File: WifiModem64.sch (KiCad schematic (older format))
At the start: 4 parts, among them J1 C64-UserPort, J2 PWR1, U1 WeMos_mini, U2 WeMos_D1_mini_OLED_Shield

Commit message: WiP.
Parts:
- removed J2: PWR1, Pin_Headers:Pin_Header_Straight_1x02_Pitch2.54mm, symbol Conn_01x02
- added JP1: IntPwr, Connectors:GS2, symbol Jumper_NC_Small
- added JP2: CTS, Connectors:GS2, symbol Jumper_NC_Small
- added JP3: RTS, Connectors:GS2, symbol Jumper_NC_Small
- added JP4: SP1, Connectors:GS2, symbol Jumper_NC_Small
- added JP5: SP2, Connectors:GS2, symbol Jumper_NC_Small
- added Q1, Q2, Q3, Q4: BSS138, TO_SOT_Packages_SMD:SOT-23, symbol BSS138
- added R1, R2, R3, R4, R5, R6, R7, R8: 10k, Resistors_SMD:R_0805_HandSoldering, symbol R
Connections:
- net labels added: +3V3, CTS, RTS, SP1, SP2
- net labels removed: W_3V3, W_5V, W_GND
- wire segments 27 -> 71
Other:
- moved on the sheet: J1

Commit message: WiP.
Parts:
- added SW1: Push, Buttons_Switches_THT:SW_Tactile_SPST_Angled_PTS645Vx58-2LFS, symbol SW_Push
- added SW2: Reset, Buttons_Switches_THT:SW_Tactile_SPST_Angled_PTS645Vx58-2LFS, symbol SW_Push
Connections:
- net GND: now also SW1.2, SW2.2
- net W_D3: now also SW1.1
- net RST: now reaches J1.3 (/RST)
- net RST: now also SW2.1
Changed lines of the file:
@@
 	1    0    0    -1
 $EndComp
-Wire Wire Line
-	6550 3550 7200 3550
 $Comp
 L +5V #PWR03
@@
 	1    0    0    -1
 $EndComp
-Wire Wire Line
-	5500 3650 5550 3650
-Wire Wire Line
-	5450 3550 5550 3550
-Wire Wire Line
-	5550 4350 5150 4350
-Wire Wire Line
-	5150 4350 5150 4900
-Wire Wire Line
-	5150 4900 6650 4900
-Wire Wire Line
-	6650 4900 6650 3950
-Wire Wire Line
-	6650 3950 6550 3950
-Wire Wire Line
-	6550 3850 6700 3850
-Wire Wire Line
-	6700 4050 6550 4050
-Wire Wire Line
-	5400 4600 5400 4550
-Wire Wire Line
-	5400 4550 5550 4550
 $Comp
 L WeMos_D1_mini_OLED_Shield U2
@@
 Text GLabel 5450 3550 0    39   Input ~ 0
 SP2
-Wire Wire Line
-	5500 3650 5500 3550
-Connection ~ 5500 3550
 Text GLabel 5450 4250 0    39   Input ~ 0
 RTS
-Wire Wire Line
-	5450 4250 5550 4250
 Text GLabel 5450 3750 0    39   Input ~ 0
 CTS
-Wire Wire Line
-	5450 3750 5550 3750
 Text GLabel 6700 4050 2    39   Input ~ 0
 SP2
 Text GLabel 5450 4450 0    39   Input ~ 0
 SP1
-Wire Wire Line
-	5450 4450 5550 4450
 Text GLabel 6700 3850 2    39   Input ~ 0
 SP1
-Wire Wire Line
-	6550 4550 6550 4650
-Wire Wire Line
-	6550 4650 5500 4650
-Wire Wire Line
-	5500 4650 5500 4550
-Connection ~ 5500 4550
-Wire Wire Line
-	6550 3300 6550 3450
-Wire Wire Line
-	5450 3300 6550 3300
-Wire Wire Line
-	5550 3300 5550 3450
 $Comp
 L GND #PWR05
@@
 	1    0    0    -1
 $EndComp
-Connection ~ 5550 3300
 $Comp
 L Jumper_NC_Small JP1
@@
 	1    0    0    -1
 $EndComp
-Wire Wire Line
-	7400 3550 7400 3450
 $Comp
 L +3V3 #PWR06
@@
 	1    0    0    -1
 $EndComp
-Wire Wire Line
-	3700 1450 3800 1450
-Wire Wire Line
-	3800 1450 3800 1400
 $Comp
 L +3V3 #PWR07
@@
 	1    0    0    -1
 $EndComp
-Wire Wire Line
-	5750 1450 5850 1450
-Wire Wire Line
-	5850 1450 5850 1400
-Wire Wire Line
-	2700 1550 2350 1550
-Wire Wire Line
-	2350 1550 2350 1600
-Wire Wire Line
-	2700 1450 2600 1450
-Wire Wire Line
-	2600 1450 2600 1400
 $Comp
 L +5V #PWR08
@@
 	1    0    0    -1
 $EndComp
-Wire Wire Line
-	4750 1450 4650 1450
-Wire Wire Line
-	4650 1450 4650 1400
 $Comp
 L GND #PWR09
@@
 	1    0    0    -1
 $EndComp
-Wire Wire Line
-	4750 1550 4400 1550
-Wire Wire Line
-	4400 1550 4400 1600
 $Comp
 L Jumper_NC_Small JP5
@@
 Text GLabel 9700 6000 0    39   Input ~ 0
 SP2
-Wire Wire Line
-	9700 6000 9800 6000
 Text GLabel 10350 6000 2    39   Input ~ 0
 W_TX
-Wire Wire Line
-	10000 6000 10350 6000
 $Comp
 L BSS138 Q4
@@
 	1    0    0    -1
 $EndComp
-Wire Wire Line
-	9750 5650 9800 5650
-Wire Wire Line
-	10200 5650 10250 5650
-Wire Wire Line
-	9750 5350 10000 5350
 $Comp
 L +3V3 #PWR010
@@
 	1    0    0    -1
 $EndComp
-Wire Wire Line
-	9750 5350 9750 5300
-Wire Wire Line
-	10250 5300 10250 5350
-Wire Wire Line
-	9750 5650 9750 6000
-Connection ~ 9750 6000
-Wire Wire Line
-	10250 5650 10250 6000
-Connection ~ 10250 6000
 $Comp
 L Jumper_NC_Small JP4
@@
 Text GLabel 9700 4950 0    39   Input ~ 0
 SP1
-Wire Wire Line
-	9700 4950 9800 4950
 Text GLabel 10350 4950 2    39   Input ~ 0
 W_RX
-Wire Wire Line
-	10000 4950 10350 4950
 $Comp
 L BSS138 Q3
@@
 	1    0    0    -1
 $EndComp
-Wire Wire Line
-	9750 4600 9800 4600
-Wire Wire Line
-	10200 4600 10250 4600
-Wire Wire Line
-	9750 4300 10000 4300
 $Comp
 L +3V3 #PWR012
@@
 	1    0    0    -1
 $EndComp
-Wire Wire Line
-	9750 4300 9750 4250
-Wire Wire Line
-	10250 4250 10250 4300
-Wire Wire Line
-	9750 4600 9750 4950
-Connection ~ 9750 4950
-Wire Wire Line
-	10250 4600 10250 4950
-Connection ~ 10250 4950
 $Comp
 L Jumper_NC_Small JP3
@@
 Text GLabel 9700 3900 0    39   Input ~ 0
 RTS
-Wire Wire Line
-	9700 3900 9800 3900
 Text GLabel 10350 3900 2    39   Input ~ 0
 W_D7
-Wire Wire Line
-	10000 3900 10350 3900
 $Comp
 L BSS138 Q2
@@
 	1    0    0    -1
 $EndComp
-Wire Wire Line
-	9750 3550 9800 3550
-Wire Wire Line
-	10200 3550 10250 3550
-Wire Wire Line
-	9750 3250 10000 3250
 $Comp
 L +3V3 #PWR014
@@
 	1    0    0    -1
 $EndComp
-Wire Wire Line
-	9750 3250 9750 3200
-Wire Wire Line
-	10250 3200 10250 3250
-Wire Wire Line
-	9750 3550 9750 3900
-Connection ~ 9750 3900
-Wire Wire Line
-	10250 3550 10250 3900
-Connection ~ 10250 3900
 $Comp
 L Jumper_NC_Small JP2
@@
 Text GLabel 9700 2850 0    39   Input ~ 0
 CTS
-Wire Wire Line
-	9700 2850 9800 2850
 Text GLabel 10350 2850 2    39   Input ~ 0
 W_D6
-Wire Wire Line
-	10000 2850 10350 2850
 $Comp
 L BSS138 Q1
@@
 	1    0    0    -1
 $EndComp
-Wire Wire Line
-	9750 2500 9800 2500
-Wire Wire Line
-	10200 2500 10250 2500
-Wire Wire Line
-	9750 2200 10000 2200
 $Comp
 L +3V3 #PWR016
@@
 	1    0    0    -1
 $EndComp
+$Comp
+L SW_Push SW1
+U 1 1 5A3679A2
+P 10050 1200
+F 0 "SW1" H 10100 1300 50  0000 L CNN
+F 1 "Push" H 10050 1140 50  0000 C CNN
+F 2 "Buttons_Switches_THT:SW_Tactile_SPST_Angled_PTS645Vx58-2LFS" H 10050 1400 50  0001 C CNN
+F 3 "" H 10050 1400 50  0001 C CNN
+	1    10050 1200
+	1    0    0    -1
+$EndComp
+Text GLabel 9750 1200 0    39   Input ~ 0
+W_D3
+$Comp
+L GND #PWR018
+U 1 1 5A367D37
+P 10350 1550
+F 0 "#PWR018" H 10350 1300 50  0001 C CNN
+F 1 "GND" H 10350 1400 50  0000 C CNN
+F 2 "" H 10350 1550 50  0001 C CNN
+F 3 "" H 10350 1550 50  0001 C CNN
+	1    10350 1550
+	1    0    0    -1
+$EndComp
+$Comp
+L SW_Push SW2
+U 1 1 5A36803A
+P 10050 1500
+F 0 "SW2" H 10100 1600 50  0000 L CNN
+F 1 "Reset" H 10050 1440 50  0000 C CNN
+F 2 "Buttons_Switches_THT:SW_Tactile_SPST_Angled_PTS645Vx58-2LFS" H 10050 1700 50  0001 C CNN
+F 3 "" H 10050 1700 50  0001 C CNN
+	1    10050 1500
+	1    0    0    -1
+$EndComp
+Wire Wire Line
+	6550 3550 7200 3550
+Wire Wire Line
+	5500 3650 5550 3650
+Wire Wire Line
+	5450 3550 5550 3550
+Wire Wire Line
+	5550 4350 5150 4350
+Wire Wire Line
+	5150 4350 5150 4900
+Wire Wire Line
+	5150 4900 6650 4900
+Wire Wire Line
+	6650 4900 6650 3950
+Wire Wire Line
+	6650 3950 6550 3950
+Wire Wire Line
+	6550 3850 6700 3850
+Wire Wire Line
+	6700 4050 6550 4050
+Wire Wire Line
+	5400 4600 5400 4550
+Wire Wire Line
+	5400 4550 5550 4550
+Wire Wire Line
+	5500 3650 5500 3550
+Connection ~ 5500 3550
+Wire Wire Line
+	5450 4250 5550 4250
+Wire Wire Line
+	5450 3750 5550 3750
+Wire Wire Line
+	5450 4450 5550 4450
+Wire Wire Line
+	6550 4550 6550 4650
+Wire Wire Line
+	6550 4650 5500 4650
+Wire Wire Line
+	5500 4650 5500 4550
+Connection ~ 5500 4550
+Wire Wire Line
+	6550 3300 6550 3450
+Wire Wire Line
+	5450 3300 6550 3300
+Wire Wire Line
+	5550 3300 5550 3450
+Connection ~ 5550 3300
+Wire Wire Line
+	7400 3550 7400 3450
+Wire Wire Line
+	3700 1450 3800 1450
+Wire Wire Line
+	3800 1450 3800 1400
+Wire Wire Line
+	5750 1450 5850 1450
+Wire Wire Line
+	5850 1450 5850 1400
+Wire Wire Line
+	2700 1550 2350 1550
+Wire Wire Line
+	2350 1550 2350 1600
+Wire Wire Line
+	2700 1450 2600 1450
+Wire Wire Line
+	2600 1450 2600 1400
+Wire Wire Line
+	4750 1450 4650 1450
+Wire Wire Line
+	4650 1450 4650 1400
+Wire Wire Line
+	4750 1550 4400 1550
+Wire Wire Line
+	4400 1550 4400 1600
+Wire Wire Line
+	9700 6000 9800 6000
+Wire Wire Line
+	10000 6000 10350 6000
+Wire Wire Line
+	9750 5650 9800 5650
+Wire Wire Line
+	10200 5650 10250 5650
+Wire Wire Line
+	9750 5350 10000 5350
+Wire Wire Line
+	9750 5350 9750 5300
+Wire Wire Line
+	10250 5300 10250 5350
+Wire Wire Line
+	9750 5650 9750 6000
+Connection ~ 9750 6000
+Wire Wire Line
+	10250 5650 10250 6000
+Connection ~ 10250 6000
+Wire Wire Line
+	9700 4950 9800 4950
+Wire Wire Line
+	10000 4950 10350 4950
+Wire Wire Line
+	9750 4600 9800 4600
+Wire Wire Line
+	10200 4600 10250 4600
+Wire Wire Line
+	9750 4300 10000 4300
+Wire Wire Line
+	9750 4300 9750 4250
+Wire Wire Line
+	10250 4250 10250 4300
+Wire Wire Line
+	9750 4600 9750 4950
+Connection ~ 9750 4950
+Wire Wire Line
+	10250 4600 10250 4950
+Connection ~ 10250 4950
+Wire Wire Line
+	9700 3900 9800 3900
+Wire Wire Line
+	10000 3900 10350 3900
+Wire Wire Line
+	9750 3550 9800 3550
+Wire Wire Line
+	10200 3550 10250 3550
+Wire Wire Line
+	9750 3250 10000 3250
+Wire Wire Line
+	9750 3250 9750 3200
+Wire Wire Line
+	10250 3200 10250 3250
+Wire Wire Line
+	9750 3550 9750 3900
+Connection ~ 9750 3900
+Wire Wire Line
+	10250 3550 10250 3900
+Connection ~ 10250 3900
+Wire Wire Line
+	9700 2850 9800 2850
+Wire Wire Line
+	10000 2850 10350 2850
+Wire Wire Line
+	9750 2500 9800 2500
+Wire Wire Line
+	10200 2500 10250 2500
+Wire Wire Line
+	9750 2200 10000 2200
 Wire Wire Line
 	9750 2200 9750 2150
@@
 	10250 2500 10250 2850
 Connection ~ 10250 2850
+Wire Wire Line
+	9750 1200 9850 1200
+Wire Wire Line
+	10250 1200 10350 1200
+Wire Wire Line
+	10350 1200 10350 1550
+Wire Wire Line
+	10250 1500 10350 1500
+Connection ~ 10350 1500
+Text GLabel 9750 1500 0    39   Input ~ 0
+RST
+Wire Wire Line
+	9750 1500 9850 1500
+Text GLabel 6700 3650 2    39   Input ~ 0
+RST
+Wire Wire Line
+	6550 3650 6700 3650
 $EndSCHEMATC

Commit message: Added LED and mounting holes.
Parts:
- added C1: 100n, Capacitors_SMD:C_0805_HandSoldering, symbol C
- added LED1: WS2812B, WifiModem64:WS2812B, symbol WS2812B
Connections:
- net +5V: now also C1.1, LED1.1 (VCC)
- net GND: now also C1.2, LED1.3 (GND)
- net W_D0: now also LED1.4 (DIN)
- net W_D7: no longer JP3.2, Q2.3 (D), R6.2
- net W_D8: now also JP3.2, Q2.3 (D), R6.2
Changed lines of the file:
@@
 RTS
 Text GLabel 10350 3900 2    39   Input ~ 0
-W_D7
+W_D8
 $Comp
 L BSS138 Q2
@@
 Wire Wire Line
 	6550 3650 6700 3650
+$Comp
+L GND #PWR019
+U 1 1 5A378519
+P 3800 4150
+F 0 "#PWR019" H 3800 3900 50  0001 C CNN
+F 1 "GND" H 3800 4000 50  0000 C CNN
+F 2 "" H 3800 4150 50  0001 C CNN
+F 3 "" H 3800 4150 50  0001 C CNN
+	1    3800 4150
+	1    0    0    -1
+$EndComp
+$Comp
+L +5V #PWR020
+U 1 1 5A37855B
+P 2500 3750
+F 0 "#PWR020" H 2500 3600 50  0001 C CNN
+F 1 "+5V" H 2500 3890 50  0000 C CNN
+F 2 "" H 2500 3750 50  0001 C CNN
+F 3 "" H 2500 3750 50  0001 C CNN
+	1    2500 3750
+	1    0    0    -1
+$EndComp
+Text GLabel 3650 3750 2    39   Input ~ 0
+W_D0
+$Comp
+L WS2812B LED1
+U 1 1 5A3787C4
+P 3150 3950
+F 0 "LED1" H 3150 3550 60  0000 C CNN
+F 1 "WS2812B" H 3150 4350 60  0000 C CNN
+F 2 "WifiModem64:WS2812B" V 3100 3950 60  0001 C CNN
+F 3 "" V 3100 3950 60  0000 C CNN
+	1    3150 3950
+	1    0    0    -1
+$EndComp
+Wire Wire Line
+	2500 3750 2650 3750
+Wire Wire Line
+	3650 4150 3800 4150
+$Comp
+L C C1
+U 1 1 5A3799FA
+P 2550 3950
+F 0 "C1" H 2575 4050 50  0000 L CNN
+F 1 "100n" H 2575 3850 50  0000 L CNN
+F 2 "Capacitors_SMD:C_0805_HandSoldering" H 2588 3800 50  0001 C CNN
+F 3 "" H 2550 3950 50  0001 C CNN
+	1    2550 3950
+	1    0    0    -1
+$EndComp
+Wire Wire Line
+	2550 3800 2550 3750
+Connection ~ 2550 3750
+Wire Wire Line
+	2550 4100 2550 4450
+Wire Wire Line
+	2550 4450 3700 4450
+Wire Wire Line
+	3700 4450 3700 4150
+Connection ~ 3700 4150
 $EndSCHEMATC

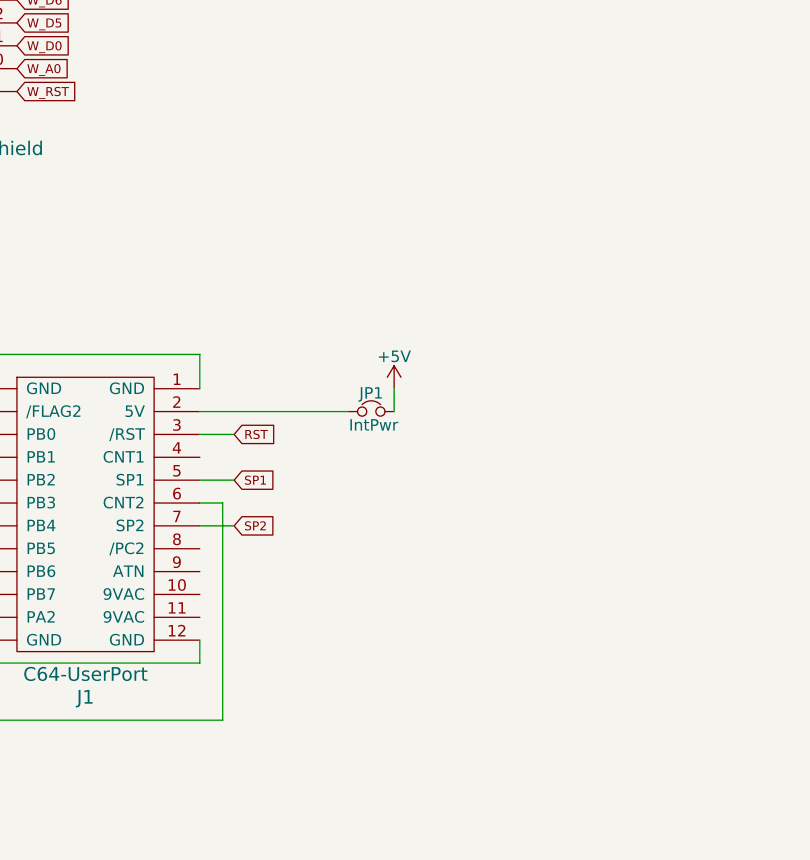
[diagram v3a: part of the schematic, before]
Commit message: Added optional USB power supply.
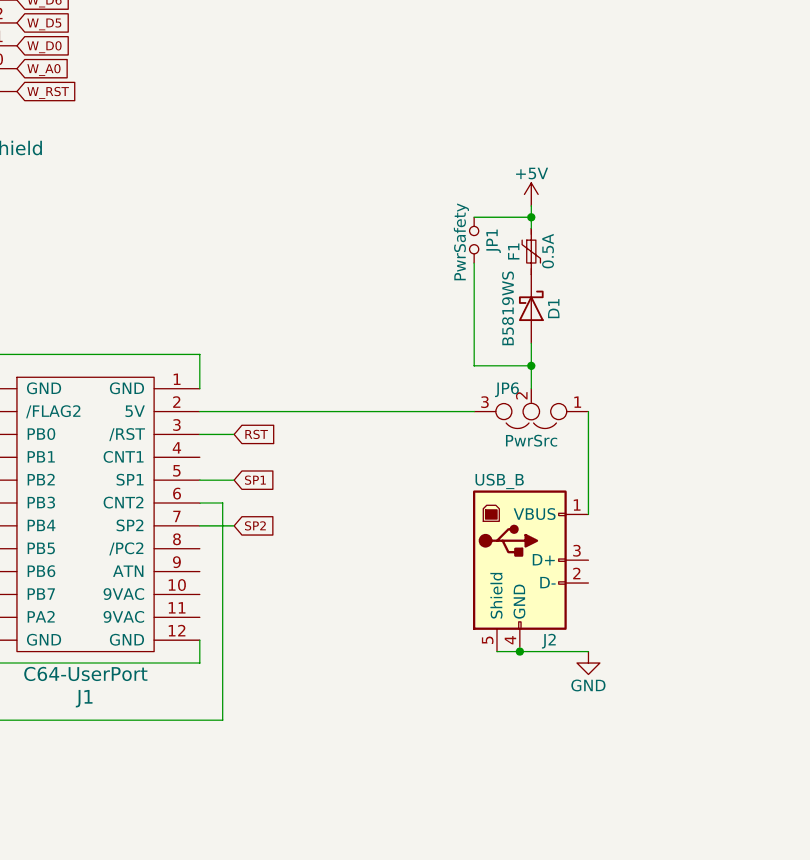
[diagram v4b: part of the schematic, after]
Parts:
- removed JP1: IntPwr, Connectors:GS2, symbol Jumper_NC_Small
- added D1: B5819WS, Diodes_SMD:D_0805, symbol D_Schottky
- added F1: 0.5A, Resistors_SMD:R_1206_HandSoldering, symbol Polyfuse_Small
- added J2: USB_B, Connectors:USB_Micro-B, symbol USB_B
- added JP1: PwrSafety, Connectors:GS2, symbol Jumper_NO_Small
- added JP6: PwrSrc, Pin_Headers:Pin_Header_Straight_1x03_Pitch2.54mm, symbol Jumper_NC_Dual
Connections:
- net +5V: now also F1.1, JP1.1
- net GND: now also J2.4 (GND), J2.5 (Shield)
- net at J1.2 (5V): now also JP6.3
- new net: D1.1 (K), F1.2
- new net: D1.2 (A), JP1.2, JP6.2
- new net: J2.1 (VBUS), JP6.1
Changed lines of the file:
@@
 encoding utf-8
 Sheet 1 1
-Title ""
-Date ""
-Rev ""
-Comp ""
+Title "WifiModem64"
+Date "2017-12-18"
+Rev "1.0"
+Comp "hackup.net"
 Comment1 ""
 Comment2 ""
@@
 $Comp
 L +5V #PWR02
-U 1 1 5A282304
-P 7400 3450
-F 0 "#PWR02" H 7400 3300 50  0001 C CNN
-F 1 "+5V" H 7400 3590 50  0000 C CNN
-F 2 "" H 7400 3450 50  0001 C CNN
-F 3 "" H 7400 3450 50  0001 C CNN
-	1    7400 3450
-	1    0    0    -1
-$EndComp
-$Comp
-L +5V #PWR03
 U 1 1 5A282331
 P 2600 1400
-F 0 "#PWR03" H 2600 1250 50  0001 C CNN
+F 0 "#PWR02" H 2600 1250 50  0001 C CNN
 F 1 "+5V" H 2600 1540 50  0000 C CNN
 F 2 "" H 2600 1400 50  0001 C CNN
@@
 $EndComp
 $Comp
-L GND #PWR04
+L GND #PWR03
 U 1 1 5A282352
 P 2350 1600
-F 0 "#PWR04" H 2350 1350 50  0001 C CNN
+F 0 "#PWR03" H 2350 1350 50  0001 C CNN
 F 1 "GND" H 2350 1450 50  0000 C CNN
 F 2 "" H 2350 1600 50  0001 C CNN
@@
 SP1
 $Comp
-L GND #PWR05
+L GND #PWR04
 U 1 1 5A292D50
 P 5450 3300
-F 0 "#PWR05" H 5450 3050 50  0001 C CNN
+F 0 "#PWR04" H 5450 3050 50  0001 C CNN
 F 1 "GND" H 5450 3150 50  0000 C CNN
 F 2 "" H 5450 3300 50  0001 C CNN
@@
 $EndComp
 $Comp
-L Jumper_NC_Small JP1
-U 1 1 5A358E3E
-P 7300 3550
-F 0 "JP1" H 7300 3630 50  0000 C CNN
-F 1 "IntPwr" H 7310 3490 50  0000 C CNN
-F 2 "Connectors:GS2" H 7300 3550 50  0001 C CNN
-F 3 "" H 7300 3550 50  0001 C CNN
-	1    7300 3550
-	1    0    0    -1
-$EndComp
-$Comp
-L +3V3 #PWR06
+L +3V3 #PWR05
 U 1 1 5A364EDA
 P 3800 1400
-F 0 "#PWR06" H 3800 1250 50  0001 C CNN
+F 0 "#PWR05" H 3800 1250 50  0001 C CNN
 F 1 "+3V3" H 3800 1540 50  0000 C CNN
 F 2 "" H 3800 1400 50  0001 C CNN
@@
 $EndComp
 $Comp
-L +3V3 #PWR07
+L +3V3 #PWR06
 U 1 1 5A36503E
 P 5850 1400
-F 0 "#PWR07" H 5850 1250 50  0001 C CNN
+F 0 "#PWR06" H 5850 1250 50  0001 C CNN
 F 1 "+3V3" H 5850 1540 50  0000 C CNN
 F 2 "" H 5850 1400 50  0001 C CNN
@@
 $EndComp
 $Comp
-L +5V #PWR08
+L +5V #PWR07
 U 1 1 5A365155
 P 4650 1400
-F 0 "#PWR08" H 4650 1250 50  0001 C CNN
+F 0 "#PWR07" H 4650 1250 50  0001 C CNN
 F 1 "+5V" H 4650 1540 50  0000 C CNN
 F 2 "" H 4650 1400 50  0001 C CNN
@@
 $EndComp
 $Comp
-L GND #PWR09
+L GND #PWR08
 U 1 1 5A36519A
 P 4400 1600
-F 0 "#PWR09" H 4400 1350 50  0001 C CNN
+F 0 "#PWR08" H 4400 1350 50  0001 C CNN
 F 1 "GND" H 4400 1450 50  0000 C CNN
 F 2 "" H 4400 1600 50  0001 C CNN
@@
 $EndComp
 $Comp
-L +3V3 #PWR010
+L +3V3 #PWR09
 U 1 1 5A3655FB
 P 9750 5300
-F 0 "#PWR010" H 9750 5150 50  0001 C CNN
+F 0 "#PWR09" H 9750 5150 50  0001 C CNN
 F 1 "+3V3" H 9750 5440 50  0000 C CNN
 F 2 "" H 9750 5300 50  0001 C CNN
@@
 $EndComp
 $Comp
-L +5V #PWR011
+L +5V #PWR010
 U 1 1 5A36561F
 P 10250 5300
-F 0 "#PWR011" H 10250 5150 50  0001 C CNN
+F 0 "#PWR010" H 10250 5150 50  0001 C CNN
 F 1 "+5V" H 10250 5440 50  0000 C CNN
 F 2 "" H 10250 5300 50  0001 C CNN
@@
 $EndComp
 $Comp
-L +3V3 #PWR012
+L +3V3 #PWR011
 U 1 1 5A365F86
 P 9750 4250
-F 0 "#PWR012" H 9750 4100 50  0001 C CNN
+F 0 "#PWR011" H 9750 4100 50  0001 C CNN
 F 1 "+3V3" H 9750 4390 50  0000 C CNN
 F 2 "" H 9750 4250 50  0001 C CNN
@@
 $EndComp
 $Comp
-L +5V #PWR013
+L +5V #PWR012
 U 1 1 5A365F8C
 P 10250 4250
-F 0 "#PWR013" H 10250 4100 50  0001 C CNN
+F 0 "#PWR012" H 10250 4100 50  0001 C CNN
 F 1 "+5V" H 10250 4390 50  0000 C CNN
 F 2 "" H 10250 4250 50  0001 C CNN
@@
 $EndComp
 $Comp
-L +3V3 #PWR014
+L +3V3 #PWR013
 U 1 1 5A366337
 P 9750 3200
-F 0 "#PWR014" H 9750 3050 50  0001 C CNN
+F 0 "#PWR013" H 9750 3050 50  0001 C CNN
 F 1 "+3V3" H 9750 3340 50  0000 C CNN
 F 2 "" H 9750 3200 50  0001 C CNN
@@
 $EndComp
 $Comp
-L +5V #PWR015
+L +5V #PWR014
 U 1 1 5A36633D
 P 10250 3200
-F 0 "#PWR015" H 10250 3050 50  0001 C CNN
+F 0 "#PWR014" H 10250 3050 50  0001 C CNN
 F 1 "+5V" H 10250 3340 50  0000 C CNN
 F 2 "" H 10250 3200 50  0001 C CNN
@@
 $EndComp
 $Comp
-L +3V3 #PWR016
+L +3V3 #PWR015
 U 1 1 5A366444
 P 9750 2150
-F 0 "#PWR016" H 9750 2000 50  0001 C CNN
+F 0 "#PWR015" H 9750 2000 50  0001 C CNN
 F 1 "+3V3" H 9750 2290 50  0000 C CNN
 F 2 "" H 9750 2150 50  0001 C CNN
@@
 $EndComp
 $Comp
-L +5V #PWR017
+L +5V #PWR016
 U 1 1 5A36644A
 P 10250 2150
-F 0 "#PWR017" H 10250 2000 50  0001 C CNN
+F 0 "#PWR016" H 10250 2000 50  0001 C CNN
 F 1 "+5V" H 10250 2290 50  0000 C CNN
 F 2 "" H 10250 2150 50  0001 C CNN
@@
 W_D3
 $Comp
-L GND #PWR018
+L GND #PWR017
 U 1 1 5A367D37
 P 10350 1550
-F 0 "#PWR018" H 10350 1300 50  0001 C CNN
+F 0 "#PWR017" H 10350 1300 50  0001 C CNN
 F 1 "GND" H 10350 1400 50  0000 C CNN
 F 2 "" H 10350 1550 50  0001 C CNN
@@
 $EndComp
 Wire Wire Line
-	6550 3550 7200 3550
-Wire Wire Line
 	5500 3650 5550 3650
 Wire Wire Line
@@
 	5550 3300 5550 3450
 Connection ~ 5550 3300
-Wire Wire Line
-	7400 3550 7400 3450
 Wire Wire Line
 	3700 1450 3800 1450
@@
 	6550 3650 6700 3650
 $Comp
-L GND #PWR019
+L GND #PWR018
 U 1 1 5A378519
 P 3800 4150
-F 0 "#PWR019" H 3800 3900 50  0001 C CNN
+F 0 "#PWR018" H 3800 3900 50  0001 C CNN
 F 1 "GND" H 3800 4000 50  0000 C CNN
 F 2 "" H 3800 4150 50  0001 C CNN
@@
 $EndComp
 $Comp
-L +5V #PWR020
+L +5V #PWR019
 U 1 1 5A37855B
 P 2500 3750
-F 0 "#PWR020" H 2500 3600 50  0001 C CNN
+F 0 "#PWR019" H 2500 3600 50  0001 C CNN
 F 1 "+5V" H 2500 3890 50  0000 C CNN
 F 2 "" H 2500 3750 50  0001 C CNN
@@
 	3700 4450 3700 4150
 Connection ~ 3700 4150
+$Comp
+L +5V #PWR020
+U 1 1 5A37B010
+P 8000 2650
+F 0 "#PWR020" H 8000 2500 50  0001 C CNN
+F 1 "+5V" H 8000 2790 50  0000 C CNN
+F 2 "" H 8000 2650 50  0001 C CNN
+F 3 "" H 8000 2650 50  0001 C CNN
+	1    8000 2650
+	1    0    0    -1
+$EndComp
+$Comp
+L D_Schottky D1
+U 1 1 5A37B054
+P 8000 3100
+F 0 "D1" H 8000 3200 50  0000 C CNN
+F 1 "B5819WS" H 8000 3000 50  0000 C CNN
+F 2 "Diodes_SMD:D_0805" H 8000 3100 50  0001 C CNN
+F 3 "" H 8000 3100 50  0001 C CNN
+	1    8000 3100
+	0    1    1    0
+$EndComp
+$Comp
+L Polyfuse_Small F1
+U 1 1 5A37B0D5
+P 8000 2850
+F 0 "F1" V 7925 2850 50  0000 C CNN
+F 1 "0.5A" V 8075 2850 50  0000 C CNN
+F 2 "Resistors_SMD:R_1206_HandSoldering" H 8050 2650 50  0001 L CNN
+F 3 "" H 8000 2850 50  0001 C CNN
+	1    8000 2850
+	1    0    0    -1
+$EndComp
+$Comp
+L Jumper_NO_Small JP1
+U 1 1 5A37B2BB
+P 7750 2800
+F 0 "JP1" H 7750 2880 50  0000 C CNN
+F 1 "PwrSafety" H 7760 2740 50  0000 C CNN
+F 2 "Connectors:GS2" H 7750 2800 50  0001 C CNN
+F 3 "" H 7750 2800 50  0001 C CNN
+	1    7750 2800
+	0    1    1    0
+$EndComp
+Wire Wire Line
+	8000 2650 8000 2750
+Wire Wire Line
+	7750 2700 8000 2700
+Connection ~ 8000 2700
+$Comp
+L USB_B J2
+U 1 1 5A37B8E2
+P 7950 4200
+F 0 "J2" H 8050 3850 50  0000 L CNN
+F 1 "USB_B" H 7750 4550 50  0000 L CNN
+F 2 "Connectors:USB_Micro-B" H 8100 4150 50  0001 C CNN
+F 3 "" H 8100 4150 50  0001 C CNN
+	1    7950 4200
+	1    0    0    -1
+$EndComp
+$Comp
+L Jumper_NC_Dual JP6
+U 1 1 5A37B9D7
+P 8000 3550
+F 0 "JP6" H 8050 3450 50  0000 L CNN
+F 1 "PwrSrc" H 8000 3650 50  0000 C BNN
+F 2 "Pin_Headers:Pin_Header_Straight_1x03_Pitch2.54mm" H 8000 3550 50  0001 C CNN
+F 3 "" H 8000 3550 50  0001 C CNN
+	1    8000 3550
+	-1   0    0    1
+$EndComp
+Wire Wire Line
+	8000 3450 8000 3250
+Wire Wire Line
+	6550 3550 7750 3550
+Wire Wire Line
+	8250 3550 8250 4000
+$Comp
+L GND #PWR021
+U 1 1 5A37BF42
+P 8250 4600
+F 0 "#PWR021" H 8250 4350 50  0001 C CNN
+F 1 "GND" H 8250 4450 50  0000 C CNN
+F 2 "" H 8250 4600 50  0001 C CNN
+F 3 "" H 8250 4600 50  0001 C CNN
+	1    8250 4600
+	1    0    0    -1
+$EndComp
+Wire Wire Line
+	7850 4600 8250 4600
+Connection ~ 7950 4600
+Wire Wire Line
+	7750 2900 7750 3350
+Wire Wire Line
+	7750 3350 8000 3350
+Connection ~ 8000 3350
 $EndSCHEMATC
